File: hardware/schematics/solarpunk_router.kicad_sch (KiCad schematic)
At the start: 2 parts

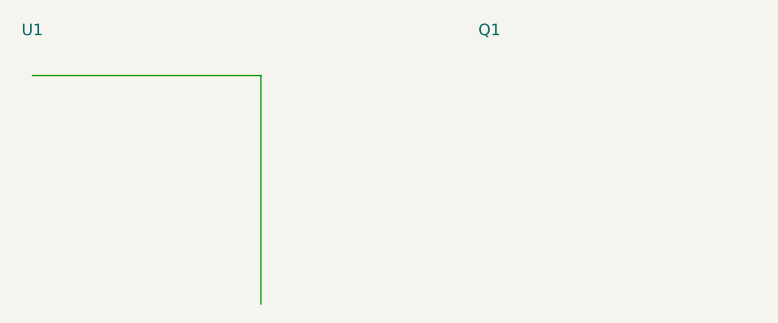
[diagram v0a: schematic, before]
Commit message: Modify schematic for solarpunk router
Updated paper size to A3 and added new components.
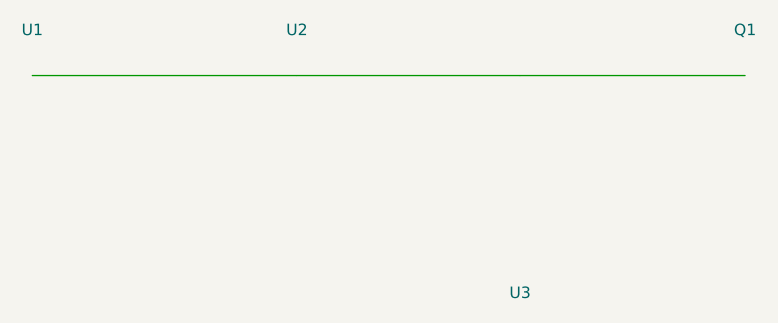
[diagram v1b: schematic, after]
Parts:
- added U2: (no value), symbol Driver:TC4420
- added U3: (no value), symbol Sensor:INA219
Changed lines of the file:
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@@
 (kicad_sch (version 20230121) (generator "eeschema")
-  (paper "A4")
-  (wire (pts (xy 50.8 50.8) (xy 76.2 50.8)) (stroke (width 0) (type default)) (uuid "wire-bus-rail-1"))
-  (wire (pts (xy 76.2 50.8) (xy 76.2 76.2)) (stroke (width 0) (type default)) (uuid "wire-bus-rail-2"))
+  (paper "A3")
+  (wire (pts (xy 50.8 50.8) (xy 80.2 50.8)) (stroke (width 0) (type default)) (uuid "wire-mcu-gate-1"))
+  (wire (pts (xy 80.2 50.8) (xy 105.0 50.8)) (stroke (width 0) (type default)) (uuid "wire-gate-driver-2"))
+  (wire (pts (xy 105.0 50.8) (xy 130.0 50.8)) (stroke (width 0) (type default)) (uuid "wire-mosfet-gate-3"))
   (symbol (lib_id "MCU_Teensy:Teensy4.1") (at 50.8 50.8 0) (unit 1)
     (uuid "sym-mcu-teensy-inst")
     (property "Reference" "U1" (at 50.8 45.72 0) (effects (font (size 1.27 1.27))))
   )
-  (symbol (lib_id "Power:MOSFET_N") (at 101.6 50.8 0) (unit 1)
+  (symbol (lib_id "Driver:TC4420") (at 80.2 50.8 0) (unit 1)
+    (uuid "sym-driver-inst")
+    (property "Reference" "U2" (at 80.2 45.72 0) (effects (font (size 1.27 1.27))))
+  )
+  (symbol (lib_id "Power:MOSFET_N") (at 130.0 50.8 0) (unit 1)
     (uuid "sym-mosfet-inst-1")
-    (property "Reference" "Q1" (at 101.6 45.72 0) (effects (font (size 1.27 1.27))))
+    (property "Reference" "Q1" (at 130.0 45.72 0) (effects (font (size 1.27 1.27))))
+  )
+  (symbol (lib_id "Sensor:INA219") (at 105.0 80.0 0) (unit 1)
+    (uuid "sym-sensor-inst")
+    (property "Reference" "U3" (at 105.0 74.93 0) (effects (font (size 1.27 1.27))))
   )
   (sheet_instances (path "/" (page 1)))
